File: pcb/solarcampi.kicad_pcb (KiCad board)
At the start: 2 copper layers, 65 x 30 mm, 53 parts, among them J1 Vin 12V, J2 AVR-ISP-6, J3 FTDI_AVR, J4 Conn_02x20_Odd_Even, J5 FTDI_RPI, J6 Shunt, Q1 Q_NMOS_GSD, Q2 IRLML 2244, Q3 Q_NMOS_GSD, Q4 Q_NMOS_GSD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

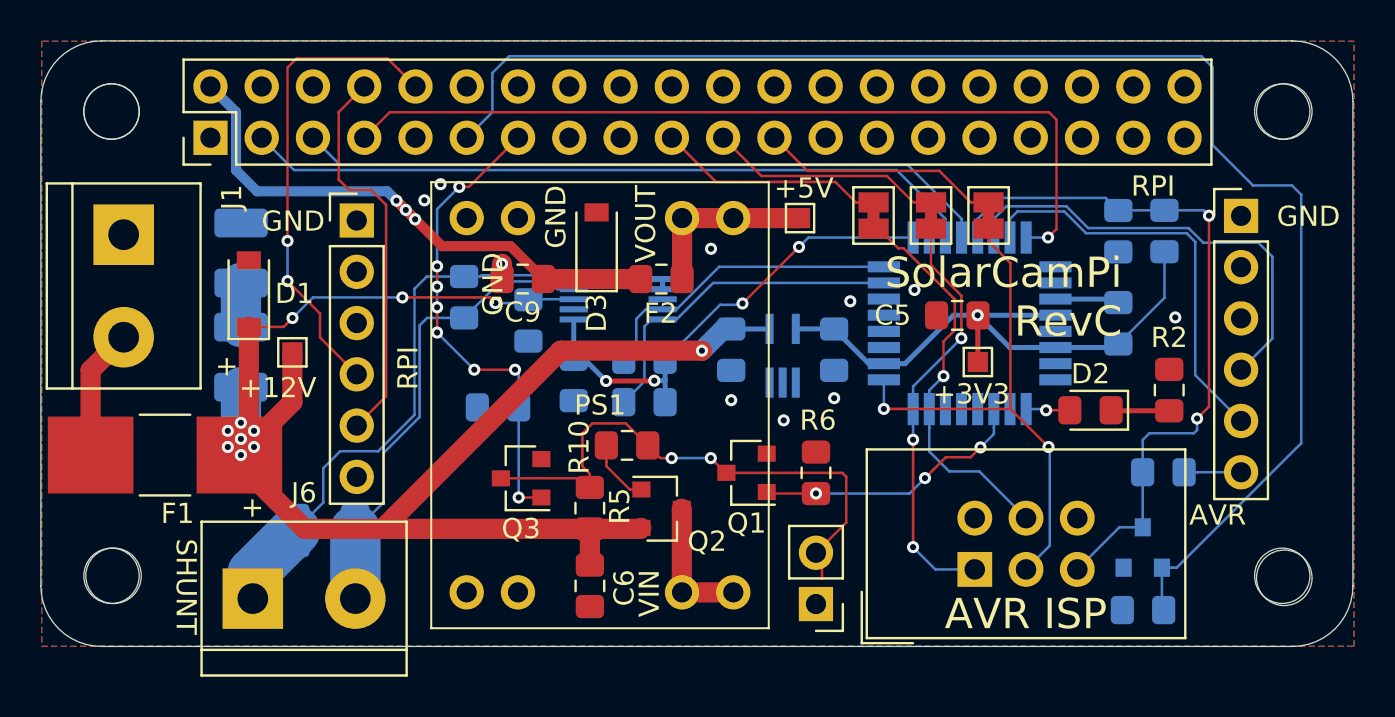
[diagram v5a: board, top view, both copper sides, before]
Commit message: Add big electrolytic cap for further suppression of ringing
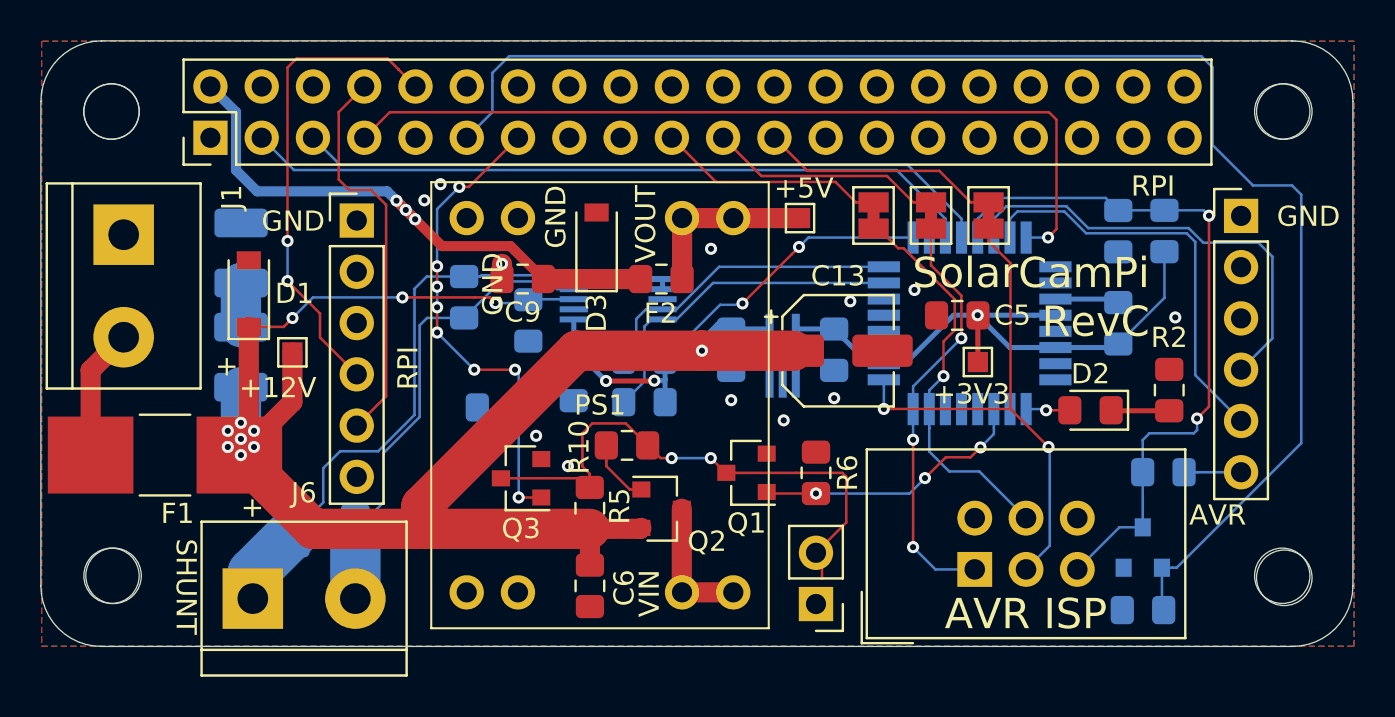
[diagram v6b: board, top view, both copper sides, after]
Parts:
- added C13: CP, Capacitor_SMD:CP_Elec_5x5.4, F.Cu at (89.5, 64.4)
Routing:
- net +12V: track 79.5 -> 83.2 mm
- net GND: vias 10 -> 12
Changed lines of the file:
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@@
     (thickness 1.6)
     (drawings 44)
-    (tracks 396)
+    (tracks 400)
     (zones 0)
-    (modules 53)
+    (modules 54)
     (nets 84)
   )
@@
   )
   (setup
-    (last_trace_width 1)
+    (last_trace_width 2)
     (user_trace_width 0.127)
     (user_trace_width 0.25)
@@
     (add_net "Net-(U3-Pad8)")
   )
+  (module Capacitor_SMD:CP_Elec_5x5.4 (layer F.Cu)
+    (at 89.495 64.352)
+    (descr "SMD capacitor, aluminum electrolytic, Nichicon, 5.0x5.4mm")
+    (tags "capacitor electrolytic")
+    (attr smd)
+    (fp_text reference C13 (at 0 -3.7) (layer F.SilkS)
+      (effects (font (size 1 1) (thickness 0.15)))
+    )
+    (fp_text value CP (at 0 3.7) (layer F.Fab)
+      (effects (font (size 1 1) (thickness 0.15)))
+    )
+    (fp_text user %R (at 0 0) (layer F.Fab)
+      (effects (font (size 1 1) (thickness 0.15)))
+    )
+    (fp_line (start -3.95 1.05) (end -2.9 1.05) (layer F.CrtYd) (width 0.05))
+    (fp_line (start -3.95 -1.05) (end -3.95 1.05) (layer F.CrtYd) (width 0.05))
+    (fp_line (start -2.9 -1.05) (end -3.95 -1.05) (layer F.CrtYd) (width 0.05))
+    (fp_line (start -2.9 1.05) (end -2.9 1.75) (layer F.CrtYd) (width 0.05))
+    (fp_line (start -2.9 -1.75) (end -2.9 -1.05) (layer F.CrtYd) (width 0.05))
+    (fp_line (start -2.9 -1.75) (end -1.75 -2.9) (layer F.CrtYd) (width 0.05))
+    (fp_line (start -2.9 1.75) (end -1.75 2.9) (layer F.CrtYd) (width 0.05))
+    (fp_line (start -1.75 -2.9) (end 2.9 -2.9) (layer F.CrtYd) (width 0.05))
+    (fp_line (start -1.75 2.9) (end 2.9 2.9) (layer F.CrtYd) (width 0.05))
+    (fp_line (start 2.9 1.05) (end 2.9 2.9) (layer F.CrtYd) (width 0.05))
+    (fp_line (start 3.95 1.05) (end 2.9 1.05) (layer F.CrtYd) (width 0.05))
+    (fp_line (start 3.95 -1.05) (end 3.95 1.05) (layer F.CrtYd) (width 0.05))
+    (fp_line (start 2.9 -1.05) (end 3.95 -1.05) (layer F.CrtYd) (width 0.05))
+    (fp_line (start 2.9 -2.9) (end 2.9 -1.05) (layer F.CrtYd) (width 0.05))
+    (fp_line (start -3.3125 -1.9975) (end -3.3125 -1.3725) (layer F.SilkS) (width 0.12))
+    (fp_line (start -3.625 -1.685) (end -3 -1.685) (layer F.SilkS) (width 0.12))
+    (fp_line (start -2.76 1.695563) (end -1.695563 2.76) (layer F.SilkS) (width 0.12))
+    (fp_line (start -2.76 -1.695563) (end -1.695563 -2.76) (layer F.SilkS) (width 0.12))
+    (fp_line (start -2.76 -1.695563) (end -2.76 -1.06) (layer F.SilkS) (width 0.12))
+    (fp_line (start -2.76 1.695563) (end -2.76 1.06) (layer F.SilkS) (width 0.12))
+    (fp_line (start -1.695563 2.76) (end 2.76 2.76) (layer F.SilkS) (width 0.12))
+    (fp_line (start -1.695563 -2.76) (end 2.76 -2.76) (layer F.SilkS) (width 0.12))
+    (fp_line (start 2.76 -2.76) (end 2.76 -1.06) (layer F.SilkS) (width 0.12))
+    (fp_line (start 2.76 2.76) (end 2.76 1.06) (layer F.SilkS) (width 0.12))
+    (fp_line (start -1.783956 -1.45) (end -1.783956 -0.95) (layer F.Fab) (width 0.1))
+    (fp_line (start -2.033956 -1.2) (end -1.533956 -1.2) (layer F.Fab) (width 0.1))
+    (fp_line (start -2.65 1.65) (end -1.65 2.65) (layer F.Fab) (width 0.1))
+    (fp_line (start -2.65 -1.65) (end -1.65 -2.65) (layer F.Fab) (width 0.1))
+    (fp_line (start -2.65 -1.65) (end -2.65 1.65) (layer F.Fab) (width 0.1))
+    (fp_line (start -1.65 2.65) (end 2.65 2.65) (layer F.Fab) (width 0.1))
+    (fp_line (start -1.65 -2.65) (end 2.65 -2.65) (layer F.Fab) (width 0.1))
+    (fp_line (start 2.65 -2.65) (end 2.65 2.65) (layer F.Fab) (width 0.1))
+    (fp_circle (center 0 0) (end 2.5 0) (layer F.Fab) (width 0.1))
+    (pad 2 smd roundrect (at 2.2 0) (size 3 1.6) (layers F.Cu F.Paste F.Mask) (roundrect_rratio 0.15625)
+      (net 1 GND))
+    (pad 1 smd roundrect (at -2.2 0) (size 3 1.6) (layers F.Cu F.Paste F.Mask) (roundrect_rratio 0.15625)
+      (net 2 +12V))
+    (model ${KISYS3DMOD}/Capacitor_SMD.3dshapes/CP_Elec_5x5.4.wrl
+      (at (xyz 0 0 0))
+      (scale (xyz 1 1 1))
+      (rotate (xyz 0 0 0))
+    )
+  )
   (module tps63070-module:TPS63070-module-compat (layer F.Cu)
     (at 77.7 67.05)
@@
     (tags "resistor handsolder")
     (attr smd)
-    (fp_text reference R6 (at -2.6 -0.1) (layer F.SilkS)
+    (fp_text reference R6 (at 0.002 -1.571 90) (layer F.SilkS)
       (effects (font (size 1 1) (thickness 0.15)))
     )
@@
     (tags "capacitor handsolder")
     (attr smd)
-    (fp_text reference C5 (at 3.2 0) (layer F.SilkS)
+    (fp_text reference C5 (at -2.73 0) (layer F.SilkS)
       (effects (font (size 1 1) (thickness 0.15)))
     )
@@
     (effects (font (size 1.5 1.5) (thickness 0.3)) (justify right mirror))
   )
-  (gr_text "SolarCamPi\nRevC\n" (at 103.57 61.7) (layer F.SilkS)
+  (gr_text "SolarCamPi\nRevC\n" (at 104.93 61.71) (layer F.SilkS)
     (effects (font (size 1.5 1.5) (thickness 0.3)) (justify right))
   )
@@
   (segment (start 72.846 60.04701) (end 72.846 60.04701) (width 1) (layer F.Cu) (net 1))
   (via (at 72.846 60.04701) (size 0.6) (drill 0.3) (layers F.Cu B.Cu) (net 1))
+  (via (at 76.11 70.065) (size 0.6) (drill 0.3) (layers F.Cu B.Cu) (net 1))
+  (via (at 74.535 68.565) (size 0.6) (drill 0.3) (layers F.Cu B.Cu) (net 1))
   (segment (start 86.095 63.275) (end 86.1 63.27) (width 0.25) (layer B.Cu) (net 2))
   (segment (start 84.2 63.275) (end 86.095 63.275) (width 0.25) (layer B.Cu) (net 2))
@@
   (segment (start 60 69.685) (end 59.835 69.52) (width 1) (layer F.Cu) (net 2))
   (segment (start 60 69.52) (end 59.835 69.52) (width 1) (layer F.Cu) (net 2))
-  (segment (start 82.75 64.35) (end 75.75 64.35) (width 1) (layer F.Cu) (net 2))
-  (segment (start 66.975 73.125) (end 66.975 73.175) (width 1) (layer F.Cu) (net 2))
-  (segment (start 75.75 64.35) (end 66.975 73.125) (width 1) (layer F.Cu) (net 2))
-  (segment (start 77.194 73.175) (end 66.975 73.175) (width 1) (layer F.Cu) (net 2))
-  (segment (start 66.975 73.175) (end 63.075 73.175) (width 1) (layer F.Cu) (net 2))
   (segment (start 79.703 73.175) (end 79.75 73.128) (width 1) (layer F.Cu) (net 2))
   (segment (start 77.194 73.175) (end 79.703 73.175) (width 1) (layer F.Cu) (net 2))
@@
   (segment (start 72.52 61.99) (end 73.985 61.99) (width 0.127) (layer B.Cu) (net 2))
   (segment (start 63.484 61.71) (end 62.465 62.729) (width 0.127) (layer B.Cu) (net 2))
-  (segment (start 63.075 73.175) (end 60 70.1) (width 1) (layer F.Cu) (net 2))
   (segment (start 71.48 61.71) (end 72.24 61.71) (width 0.127) (layer F.Cu) (net 2))
   (segment (start 72.24 61.71) (end 72.52 61.99) (width 0.127) (layer F.Cu) (net 2))
@@
   (segment (start 67.91 61.71) (end 63.484 61.71) (width 0.127) (layer B.Cu) (net 2))
   (via (at 67.91 61.71) (size 0.6) (drill 0.3) (layers F.Cu B.Cu) (net 2))
+  (segment (start 82.752 64.352) (end 82.75 64.35) (width 2) (layer F.Cu) (net 2))
+  (segment (start 87.295 64.352) (end 82.752 64.352) (width 2) (layer F.Cu) (net 2))
+  (segment (start 63.49 73.175) (end 59.835 69.52) (width 2) (layer F.Cu) (net 2))
+  (segment (start 76.541962 64.35) (end 68.856 72.035962) (width 2) (layer F.Cu) (net 2))
+  (segment (start 82.75 64.35) (end 76.541962 64.35) (width 2) (layer F.Cu) (net 2))
+  (segment (start 68.856 73.175) (end 63.49 73.175) (width 2) (layer F.Cu) (net 2))
+  (segment (start 68.856 72.035962) (end 68.856 73.175) (width 2) (layer F.Cu) (net 2))
+  (segment (start 77.194 73.175) (end 68.856 73.175) (width 2) (layer F.Cu) (net 2))
   (segment (start 89.295 63.27) (end 89.3 63.275) (width 0.25) (layer B.Cu) (net 3))
   (segment (start 87.4 63.27) (end 89.295 63.27) (width 0.25) (layer B.Cu) (net 3))

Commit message: Optimize GND connectivity
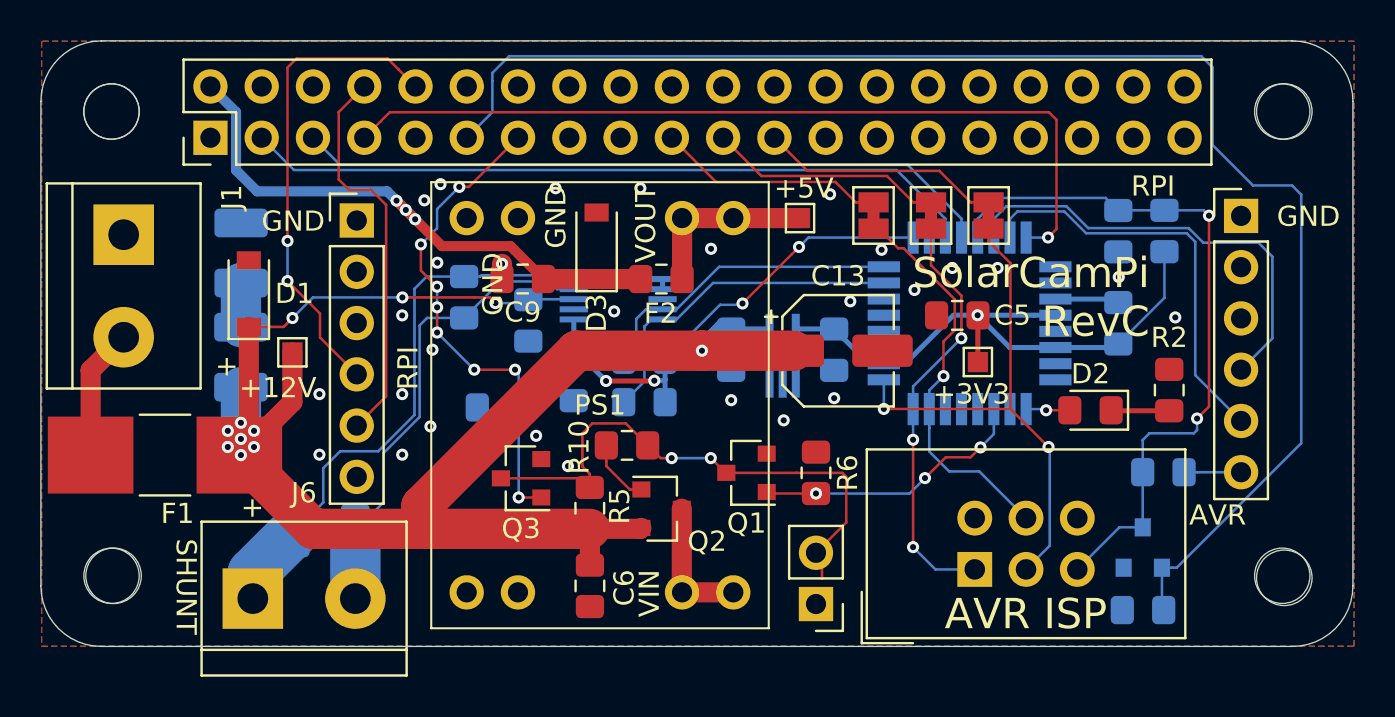
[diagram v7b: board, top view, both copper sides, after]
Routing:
- net /PWR_OVR: track 23.7 -> 24.4 mm
- net GND: vias 12 -> 28
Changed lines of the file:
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@@
     (thickness 1.6)
     (drawings 44)
-    (tracks 400)
+    (tracks 416)
     (zones 0)
     (modules 54)
@@
   )
   (setup
-    (last_trace_width 2)
+    (last_trace_width 0.127)
     (user_trace_width 0.127)
     (user_trace_width 0.25)
@@
     (tags "resistor handsolder")
     (attr smd)
-    (fp_text reference R11 (at -0.01 -2.5) (layer B.SilkS)
+    (fp_text reference R11 (at -1.03 -2.35) (layer B.SilkS)
       (effects (font (size 1 1) (thickness 0.15)) (justify mirror))
     )
@@
     (effects (font (size 1 1) (thickness 0.15)))
   )
-  (gr_text "Tobias Mädel\nTobias Schramm" (at 67.457143 72.8) (layer B.SilkS)
+  (gr_text "Tobias Mädel\nTobias Schramm" (at 67.88 72.17) (layer B.SilkS)
     (effects (font (size 1.5 1.5) (thickness 0.3)) (justify right mirror))
   )
@@
   (via (at 76.11 70.065) (size 0.6) (drill 0.3) (layers F.Cu B.Cu) (net 1))
   (via (at 74.535 68.565) (size 0.6) (drill 0.3) (layers F.Cu B.Cu) (net 1))
+  (via (at 69.64 59.99) (size 0.6) (drill 0.3) (layers F.Cu B.Cu) (net 1))
+  (via (at 63.8 66.5) (size 0.6) (drill 0.3) (layers F.Cu B.Cu) (net 1))
+  (via (at 63.8 69.5) (size 0.6) (drill 0.3) (layers F.Cu B.Cu) (net 1))
+  (via (at 67.9 69.5) (size 0.6) (drill 0.3) (layers F.Cu B.Cu) (net 1))
+  (via (at 67.9 66.5) (size 0.6) (drill 0.3) (layers F.Cu B.Cu) (net 1))
+  (via (at 69.3 68.1) (size 0.6) (drill 0.3) (layers F.Cu B.Cu) (net 1))
+  (via (at 67.9 62.6) (size 0.6) (drill 0.3) (layers F.Cu B.Cu) (net 1))
+  (via (at 69.4 64.3) (size 0.6) (drill 0.3) (layers F.Cu B.Cu) (net 1))
+  (via (at 78.4 62.4) (size 0.6) (drill 0.3) (layers F.Cu B.Cu) (net 1))
+  (via (at 79.7 56.3) (size 0.6) (drill 0.3) (layers F.Cu B.Cu) (net 1))
+  (via (at 75.5 56.3) (size 0.6) (drill 0.3) (layers F.Cu B.Cu) (net 1))
+  (via (at 89.1 56.6) (size 0.6) (drill 0.3) (layers F.Cu B.Cu) (net 1))
+  (via (at 91.65 59.35) (size 0.6) (drill 0.3) (layers F.Cu B.Cu) (net 1))
+  (via (at 97.4 60.25) (size 0.6) (drill 0.3) (layers F.Cu B.Cu) (net 1))
+  (via (at 95.15 60.25) (size 0.6) (drill 0.3) (layers F.Cu B.Cu) (net 1))
+  (via (at 103.4 60.7) (size 0.6) (drill 0.3) (layers F.Cu B.Cu) (net 1))
   (segment (start 86.095 63.275) (end 86.1 63.27) (width 0.25) (layer B.Cu) (net 2))
   (segment (start 84.2 63.275) (end 86.095 63.275) (width 0.25) (layer B.Cu) (net 2))
@@
   (segment (start 73.671 71.619) (end 73.67 71.62) (width 0.127) (layer B.Cu) (net 58))
   (segment (start 73.67 71.62) (end 74.79 71.62) (width 0.127) (layer F.Cu) (net 58))
-  (segment (start 69.629 57.333) (end 69.629 59.899) (width 0.127) (layer B.Cu) (net 58))
   (via (at 69.63 61.18) (size 0.6) (drill 0.3) (layers F.Cu B.Cu) (net 58))
   (via (at 69.63 62.2005) (size 0.6) (drill 0.3) (layers F.Cu B.Cu) (net 58))
@@
   (via (at 71.47 65.29) (size 0.6) (drill 0.3) (layers F.Cu B.Cu) (net 58))
   (segment (start 71.47 65.29) (end 73.49 65.29) (width 0.127) (layer F.Cu) (net 58))
-  (segment (start 69.629 59.899) (end 69.629 60.169) (width 0.127) (layer B.Cu) (net 58))
-  (via (at 69.63 60.17) (size 0.6) (drill 0.3) (layers F.Cu B.Cu) (net 58))
-  (segment (start 69.629 60.169) (end 69.63 60.17) (width 0.127) (layer B.Cu) (net 58))
-  (segment (start 69.63 60.17) (end 69.63 61.18) (width 0.127) (layer F.Cu) (net 58))
+  (via (at 68.827288 59.082712) (size 0.6) (drill 0.3) (layers F.Cu B.Cu) (net 58))
+  (segment (start 69.629 57.333) (end 69.629 58.281) (width 0.127) (layer B.Cu) (net 58))
+  (segment (start 69.629 58.281) (end 68.827288 59.082712) (width 0.127) (layer B.Cu) (net 58))
+  (segment (start 68.827288 60.377288) (end 69.63 61.18) (width 0.127) (layer F.Cu) (net 58))
+  (segment (start 68.827288 59.082712) (end 68.827288 60.377288) (width 0.127) (layer F.Cu) (net 58))
   (segment (start 87.427 70.4) (end 89.7 70.4) (width 0.127) (layer F.Cu) (net 66))
   (segment (start 89.7 70.4) (end 89.9 70.6) (width 0.127) (layer F.Cu) (net 66))

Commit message: Finishing touches on RevC
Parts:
- C10: value 100u -> 100µ
- C12: value C -> 100n
- C13: value CP -> 33µ
- C6: value C -> 22µ
- D3: value D_Zener -> 5.6V
- F2: value Fuse -> 1A
- JP2: value Jumper_NO_Small -> Enable RPi
- Q1, Q3, Q4: value Q_NMOS_GSD -> 2N7002
- Q2: value IRLML 2244 -> DMP3099L
- R11: value R -> .02R
- R2: value R -> 100k
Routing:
- net GND: vias 28 -> 27
